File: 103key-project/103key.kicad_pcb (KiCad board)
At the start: 2 copper layers, 207 parts, among them U1 Teensy_3.2

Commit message: Added mounting holes, cleaned up silkscreen
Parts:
- added REF**: MountingHole_5mm, Mounting_Holes:MountingHole_5mm, F.Cu at (427.0, 42.0)
- added REF**: MountingHole_5mm, Mounting_Holes:MountingHole_5mm, F.Cu at (292.0, 42.0)
- added REF**: MountingHole_5mm, Mounting_Holes:MountingHole_5mm, F.Cu at (292.0, 129.0)
- added REF**: MountingHole_5mm, Mounting_Holes:MountingHole_5mm, F.Cu at (427.0, 114.0)
- added REF**: MountingHole_5mm, Mounting_Holes:MountingHole_5mm, F.Cu at (192.0, 129.0)
- added REF**: MountingHole_5mm, Mounting_Holes:MountingHole_5mm, F.Cu at (192.0, 42.0)
- added REF**: MountingHole_5mm, Mounting_Holes:MountingHole_5mm, F.Cu at (62.0, 129.0)
- added REF**: MountingHole_5mm, Mounting_Holes:MountingHole_5mm, F.Cu at (62.0, 42.0)
- moved D93 14.4 mm to (81.2, 125.0), turned to 180 degrees
- moved D98 0.05 mm to (303.0, 128.3)
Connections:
- U1 pad GND0: (no net) -> GND
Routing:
- net R6: track 558.1 -> 575.6 mm
- net Net-(D93-Pad2): track 6.63 -> 15.7 mm
- net C12: track 271.2 -> 277.2 mm
- net C9: track 348.5 -> 353.3 mm
- net C2: track 455.4 -> 459.2 mm
- net GND: track 0.00 -> 3.73 mm, vias 0 -> 1
- net C18: track 197.0 -> 195.7 mm
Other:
- board outline added: 409.5 x 124 mm

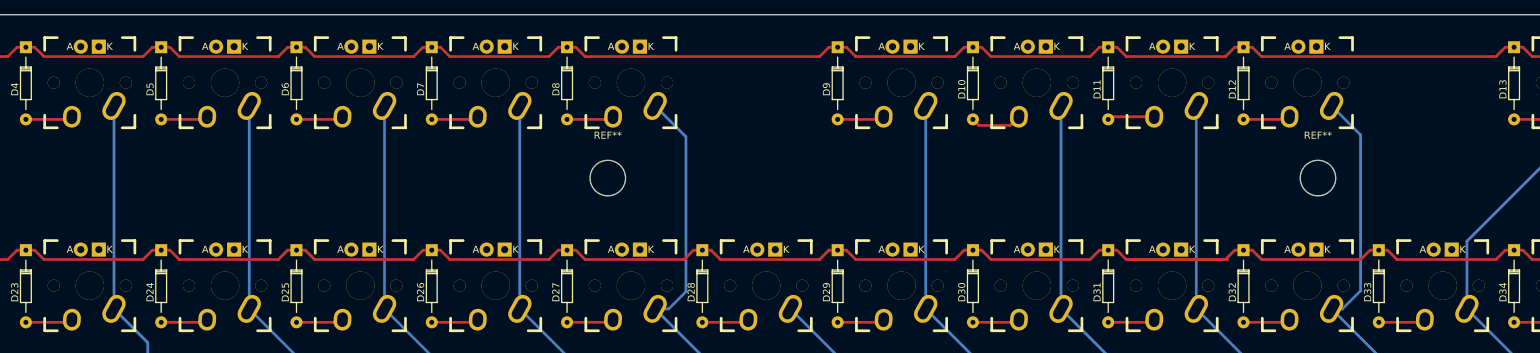
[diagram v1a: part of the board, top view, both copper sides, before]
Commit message: Updated f-row to match standard spacing
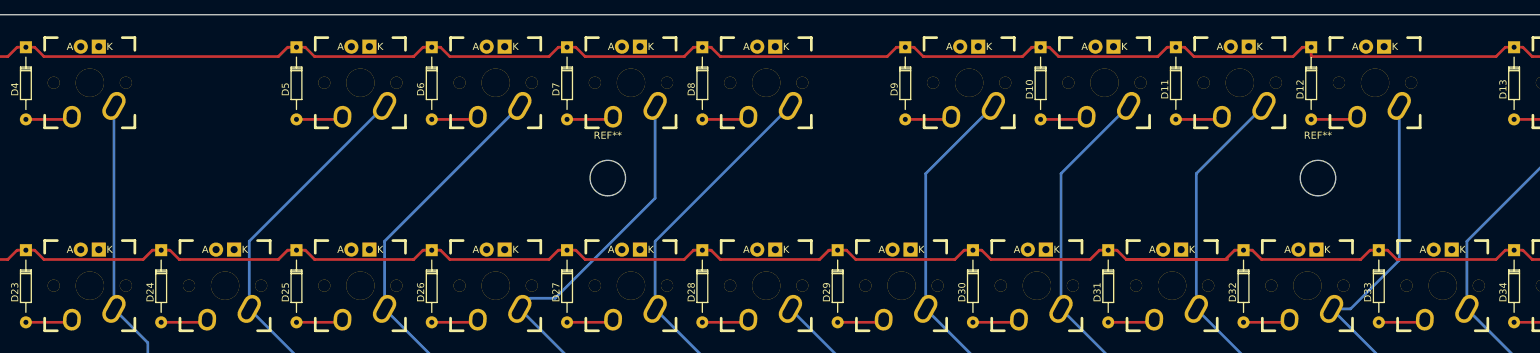
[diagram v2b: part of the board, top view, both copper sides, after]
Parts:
- moved D6 19.1 mm to (167.2, 23.6)
- moved D8 19.1 mm to (205.3, 23.6)
- moved SW_F2_6 19.1 mm to (176.2, 28.6)
- moved SW_F4_8 19.1 mm to (214.3, 28.6)
- moved D5 19.0 mm to (148.2, 23.6)
- moved D7 19.0 mm to (186.3, 23.6)
- moved SW_F1_5 19.0 mm to (157.2, 28.6)
- moved SW_F3_7 19.0 mm to (195.3, 28.6)
- moved D11 9.53 mm to (272.0, 23.6)
- moved D12 9.53 mm to (291.0, 23.6)
- moved SW_F7_11 9.53 mm to (281.0, 28.6)
- moved SW_F8_12 9.53 mm to (300.0, 28.6)
- moved D10 9.53 mm to (252.9, 23.6)
- moved SW_F6_10 9.53 mm to (261.9, 28.6)
- moved D9 9.52 mm to (233.9, 23.6)
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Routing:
- net C8: track 412.7 -> 422.6 mm
- net C7: track 380.6 -> 388.5 mm
- net C6: track 398.4 -> 406.3 mm
- net C13: track 260.2 -> 264.1 mm
- net C12: track 277.2 -> 281.1 mm
- net C11: track 389.8 -> 393.7 mm
- net C9: track 353.3 -> 356.4 mm
- net C14: track 251.4 -> 252.6 mm
- net R1: track 458.4 -> 459.1 mm
- net Net-(D10-Pad2): track 7.33 -> 6.63 mm

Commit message: Added PCB stabilizers to both 103 key and MF68+10
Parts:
- added CHERRY: MX, Cherry:CHERRY_PCB_225H_STABILIZER, F.Cu at (373.9, 95.2)
- added CHERRY: MX, Cherry:CHERRY_PCB_275H_STABILIZER, F.Cu at (369.1, 114.3)
- added CHERRY: MX, Cherry:CHERRY_PCB_200H_STABILIZER, F.Cu at (376.2, 57.1)
- added CHERRY: MX, Cherry:CHERRY_PCB_200H_STABILIZER, F.Cu at (47.6, 133.3)
- added CHERRY: MX, Cherry:CHERRY_PCB_225H_STABILIZER, F.Cu at (131.0, 114.3)
- added CHERRY: MX, Cherry:CHERRY_PCB_625H_STABILIZER, F.Cu at (240.5, 133.3)
- added STA: Stabilizer, Cherry:CHERRY_PCB_200_STABILIZER, F.Cu at (95.2, 85.7)
- added STA: Stabilizer, Cherry:CHERRY_PCB_200_STABILIZER, F.Cu at (95.2, 123.8)
- moved REF** 10.4 mm to (182.0, 132.0)
- moved REF** 10.0 mm to (182.0, 42.0)
- moved REF** 7.62 mm to (299.0, 132.0)
- moved REF** 7.00 mm to (299.0, 42.0)
- moved REF** 5.00 mm to (66.0, 132.0)
- moved REF** 4.00 mm to (66.0, 42.0)
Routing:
- net C2: track 459.2 -> 471.9 mm, vias 0 -> 1
- net R4: track 492.3 -> 481.9 mm
- net C10: track 368.3 -> 378.1 mm
- net C11: track 393.7 -> 403.4 mm
- net C9: track 356.4 -> 365.0 mm
- net C16: track 224.5 -> 229.1 mm, vias 0 -> 1
- net C15: track 252.6 -> 256.6 mm
- net GND: track 3.73 -> 0.00 mm, vias 1 -> 0
- net R6: track 575.6 -> 571.9 mm
- net C13: track 264.1 -> 260.9 mm
- net C14: track 252.6 -> 254.0 mm
- net R5: track 447.1 -> 448.3 mm
- net C8: track 422.6 -> 423.8 mm
- net C12: track 281.1 -> 282.2 mm
- net C1: track 495.1 -> 494.1 mm

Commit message: Changed key matrix to 10x11 to free up 3 teensy pins
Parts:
- added REF**: MountingHole_5mm, Mounting_Holes:MountingHole_5mm, F.Cu at (390.5, 133.2)
- U1: moved to B.Cu
- moved U1 14.9 mm to (396.7, 88.0), turned to 270 degrees
- moved REF** 10.3 mm to (76.2, 133.3)
- moved REF** 10.2 mm to (76.2, 42.9)
- moved REF** 1.65 mm to (428.6, 114.3)
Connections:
- D10 pad 1: R1 -> R2
- D100 pad 1: R6 -> R11
- D101 pad 1: R6 -> R9
- D102 pad 1: R6 -> R10
- D103 pad 1: R6 -> R11
- D12 pad 1: R1 -> R2
- D14 pad 1: R1 -> R2
- D16 pad 1: R1 -> R2
- D17 pad 1: R6 -> R1
- D18 pad 1: R6 -> R2
- D19 pad 1: R2 -> R3
- D2 pad 1: R1 -> R2
- D20 pad 1: R2 -> R4
- D21 pad 1: R2 -> R3
- D22 pad 1: R2 -> R4
- D23 pad 1: R2 -> R3
- D24 pad 1: R2 -> R4
- D25 pad 1: R2 -> R3
- D26 pad 1: R2 -> R4
- D27 pad 1: R2 -> R3
- D28 pad 1: R2 -> R4
- D29 pad 1: R2 -> R3
- D30 pad 1: R2 -> R4
- D31 pad 1: R2 -> R3
- D32 pad 1: R2 -> R4
- D33 pad 1: R2 -> R3
- D34 pad 1: R2 -> R4
- D35 pad 1: R2 -> R3
- D36 pad 1: R2 -> R4
- D37 pad 1: R6 -> R3
- D38 pad 1: R6 -> R4
- D39 pad 1: R3 -> R5
- D4 pad 1: R1 -> R2
- D40 pad 1: R3 -> R6
- D41 pad 1: R3 -> R5
- D42 pad 1: R3 -> R6
- D43 pad 1: R3 -> R5
- D44 pad 1: R3 -> R6
- D45 pad 1: R3 -> R5
- D46 pad 1: R3 -> R6
- D47 pad 1: R3 -> R5
- D48 pad 1: R3 -> R6
- D49 pad 1: R3 -> R5
- D50 pad 1: R3 -> R6
- D51 pad 1: R3 -> R5
- D52 pad 1: R3 -> R6
- D53 pad 1: R3 -> R5
- D54 pad 1: R3 -> R6
- D55 pad 1: R3 -> R5
- D56 pad 1: R3 -> R6
- D57 pad 1: R4 -> R5
- D58 pad 1: R5 -> R6
- D59 pad 1: R4 -> R7
- D6 pad 1: R1 -> R2
- D60 pad 1: R4 -> R8
- D61 pad 1: R4 -> R7
- D62 pad 1: R4 -> R7
- D63 pad 1: R4 -> R8
- D64 pad 1: R4 -> R7
- D65 pad 1: R4 -> R8
- D66 pad 1: R4 -> R7
- D67 pad 1: R4 -> R8
- D68 pad 1: R4 -> R7
- D69 pad 1: R4 -> R8
- D70 pad 1: R4 -> R7
- D71 pad 1: R4 -> R8
- D72 pad 1: R4 -> R7
- D73 pad 1: R4 -> R8
- D74 pad 1: R4 -> R7
- D75 pad 1: R5 -> R9
- D76 pad 1: R5 -> R10
- D77 pad 1: R5 -> R9
- D78 pad 1: R4 -> R8
- D79 pad 1: R5 -> R9
- D8 pad 1: R1 -> R2
- D80 pad 1: R5 -> R10
- D81 pad 1: R5 -> R9
- D82 pad 1: R5 -> R10
- D83 pad 1: R5 -> R9
- D84 pad 1: R5 -> R10
- D85 pad 1: R5 -> R9
- D86 pad 1: R5 -> R10
- D87 pad 1: R5 -> R9
- D88 pad 1: R5 -> R10
- D89 pad 1: R5 -> R9
- D90 pad 1: R5 -> R10
- D91 pad 1: R5 -> R8
- D92 pad 1: R6 -> R11
- D93 pad 1: R6 -> R11
- D94 pad 1: R6 -> R10
- D95 pad 1: R6 -> R11
- D96 pad 1: R6 -> R11
- D97 pad 1: R6 -> R11
- D98 pad 1: R6 -> R11
- D99 pad 1: R6 -> R11
- SW_2_76 pad SW1: C2 -> C1
- SW_3_77 pad SW1: C3 -> C2
- SW_5_60 pad SW1: C2 -> C1
- SW_6_61 pad SW1: C3 -> C2
- SW_8_40 pad SW1: C2 -> C1
- SW_9_41 pad SW1: C3 -> C2
- SW_A_63 pad SW1: C6 -> C3
- SW_Alt_96 pad SW1: C7 -> C4
- SW_Alt_98 pad SW1: C9 -> C6
- SW_B_84 pad SW1: C10 -> C5
- SW_Backspace_36 pad SW1: C18 -> C9
- SW_C_82 pad SW1: C8 -> C4
- SW_Caps_62 pad SW1: C5 -> C3
- SW_Ctrl_94 pad SW1: C5 -> C2
- SW_D_65 pad SW1: C8 -> C4
- SW_Del_57 pad SW1: C18 -> C10
- SW_E_46 pad SW1: C8 -> C4
- SW_End_18 pad SW1: C18 -> C9
- SW_Enter_74 pad SW1: C17 -> C9
- SW_Enter_78 pad SW1: C4 -> C2
- SW_Esc_4 pad SW1: C5 -> C2
- SW_F10_14 pad SW1: C16 -> C7
- SW_F11_15 pad SW1: C17 -> C8
- SW_F12_16 pad SW1: C18 -> C8
- SW_F1_5 pad SW1: C6 -> C3
- SW_F2_6 pad SW1: C7 -> C3
- SW_F3_7 pad SW1: C8 -> C4
- SW_F4_8 pad SW1: C9 -> C4
- SW_F5_9 pad SW1: C11 -> C5
- SW_F6_10 pad SW1: C12 -> C5
- SW_F7_11 pad SW1: C13 -> C6
- SW_F8_12 pad SW1: C14 -> C6
- SW_F9_13 pad SW1: C15 -> C7
- SW_F_66 pad SW1: C9 -> C5
- SW_G_67 pad SW1: C10 -> C5
- SW_H_68 pad SW1: C11 -> C6
- SW_Home_17 pad SW1: C17 -> C9
- SW_I_51 pad SW1: C13 -> C7
- SW_Ins_37 pad SW1: C15 -> C10
- SW_J_69 pad SW1: C12 -> C6
- SW_K_70 pad SW1: C13 -> C7
- SW_L_71 pad SW1: C14 -> C7
- SW_M_86 pad SW1: C12 -> C6
- SW_Menu_100 pad SW1: C11 -> C8
- SW_N_85 pad SW1: C11 -> C6
- SW_O_52 pad SW1: C14 -> C7
- SW_P_53 pad SW1: C15 -> C8
- SW_Pause_3 pad SW1: C3 -> C2
- SW_PgDn_58 pad SW1: C18 -> C10
- SW_PgUp_38 pad SW1: C16 -> C10
- SW_Q_44 pad SW1: C6 -> C3
- SW_R_47 pad SW1: C9 -> C5
- SW_S_64 pad SW1: C7 -> C4
- SW_Scroll_2 pad SW1: C2 -> C1
- SW_Shift_79 pad SW1: C5 -> C3
- SW_Shift_90 pad SW1: C16 -> C8
- SW_T_48 pad SW1: C10 -> C5
- SW_Tab_43 pad SW1: C5 -> C3
- SW_U_50 pad SW1: C12 -> C6
- SW_V_83 pad SW1: C9 -> C5
- SW_W_45 pad SW1: C7 -> C4
- SW_Win_95 pad SW1: C6 -> C3
- SW_Win_99 pad SW1: C10 -> C7
- SW_X10Y3_27 pad SW1: C9 -> C5
- SW_X10Y7_97 pad SW1: C8 -> C5
- SW_X11Y3_28 pad SW1: C10 -> C5
- SW_X12Y3_29 pad SW1: C11 -> C6
- SW_X13Y3_30 pad SW1: C12 -> C6
- SW_X14Y3_31 pad SW1: C13 -> C7
- SW_X15Y3_32 pad SW1: C14 -> C7
- SW_X15Y6_87 pad SW1: C13 -> C7
- SW_X16Y3_33 pad SW1: C15 -> C8
- SW_X16Y6_88 pad SW1: C14 -> C7
- SW_X17Y3_34 pad SW1: C16 -> C8
- SW_X17Y4_54 pad SW1: C16 -> C8
- SW_X17Y5_72 pad SW1: C15 -> C8
- SW_X17Y6_89 pad SW1: C15 -> C8
- SW_X18Y3_35 pad SW1: C17 -> C9
- SW_X18Y4_55 pad SW1: C17 -> C9
- SW_X18Y5_73 pad SW1: C16 -> C8
- SW_X19Y4_56 pad SW1: C18 -> C9
- SW_X20Y7_101 pad SW1: C12 -> C9
- SW_X21Y6_91 pad SW1: C17 -> C9
- SW_X21Y7_102 pad SW1: C13 -> C9
- SW_X22Y7_103 pad SW1: C14 -> C9
- SW_X3Y3_20 pad SW1: C2 -> C1
- SW_X4Y3_21 pad SW1: C3 -> C2
- SW_X4Y7_93 pad SW1: C3 -> C2
- SW_X5Y3_22 pad SW1: C4 -> C2
- SW_X5Y4_42 pad SW1: C4 -> C2
- SW_X6Y3_23 pad SW1: C5 -> C3
- SW_X7Y3_24 pad SW1: C6 -> C3
- SW_X8Y3_25 pad SW1: C7 -> C4
- SW_X9Y3_26 pad SW1: C8 -> C4
- SW_X_81 pad SW1: C7 -> C4
- SW_Y_49 pad SW1: C11 -> C6
- SW_Z_80 pad SW1: C6 -> C3
- U1 pad 10: C16 -> R4
- U1 pad 11: C17 -> R10
- U1 pad 12: C18 -> R11
- U1 pad 21: R6 -> (no net)
- U1 pad 22: R5 -> (no net)
- U1 pad 23: R4 -> (no net)
- U1 pad 5: C11 -> R9
- U1 pad 6: C12 -> R8
- U1 pad 7: C13 -> R7
- U1 pad 8: C14 -> R6
- U1 pad 9: C15 -> R5
- U1 pad GND0: GND -> (no net)
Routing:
- net R10: track 0.00 -> 456.4 mm, vias 0 -> 3
- net R9: track 0.00 -> 447.4 mm, vias 0 -> 3
- net R8: track 0.00 -> 445.2 mm, vias 0 -> 3
- net R11: track 0.00 -> 445.1 mm, vias 0 -> 1
- net C11: track 403.4 -> 0.00 mm, vias 1 -> 0
- net R7: track 0.00 -> 403.2 mm
- net C10: track 378.1 -> 70.6 mm, vias 1 -> 0
- net C12: track 282.2 -> 0.00 mm, vias 1 -> 0
- net C13: track 260.9 -> 0.00 mm, vias 1 -> 0
- net C15: track 256.6 -> 0.00 mm
- net C14: track 254.0 -> 0.00 mm, vias 1 -> 0
- net C16: track 229.1 -> 0.00 mm, vias 1 -> 0
- net C17: track 214.8 -> 0.00 mm, vias 1 -> 0
- net C18: track 195.6 -> 0.00 mm
- net R6: track 571.9 -> 410.5 mm, vias 0 -> 1
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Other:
- net class 20 added: clearance 0.2032, trace_width 0.508, via_dia 0.6096, via_drill 0.3048
- board text added: "/r/mk"
- board text added: "/u/ca178858"

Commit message: Moved diodes out of the way of the cherry stabilizers
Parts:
- moved D79 28.5 mm to (150.5, 109.3)
- moved D74 12.4 mm to (352.4, 90.2)
- moved D36 10.4 mm to (356.9, 52.1)
- moved D90 9.16 mm to (351.2, 107.3)
- moved D92 5.15 mm to (42.5, 125.0), turned to 0 degrees
- moved D97 1.64 mm to (229.9, 128.3), turned to 180 degrees
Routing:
- net Net-(D92-Pad2): track 6.63 -> 26.1 mm
- net Net-(D79-Pad2): track 6.63 -> 24.8 mm
- net Net-(D97-Pad2): track 6.63 -> 22.9 mm
- net Net-(D74-Pad2): track 6.63 -> 19.1 mm
- net Net-(D36-Pad2): track 6.63 -> 17.0 mm
- net Net-(D90-Pad2): track 6.63 -> 16.6 mm
- net R10: track 456.4 -> 454.7 mm
- net R11: track 445.1 -> 443.9 mm
